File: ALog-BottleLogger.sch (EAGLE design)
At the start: 103 parts, among them IC2 ATMEGA644M, J6 5.5x2.1mm Barrel, Q1 220mA/50V/3.5Ω, Q4 220mA/50V/3.5Ω, Q5 4.3A/20V/54mΩ, Q6 4.3A/20V/54mΩ, Q7 4.3A/20V/54mΩ, Q8 220mA/50V/3.5Ω, Q9 220mA/50V/3.5Ω, U2 FT231X-Q

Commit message: latest design files
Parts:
- removed R20, R22, R44, R45, R5: 10k, rcl:R-EU_R0603
- added ADECOUP: 0.1uF, resistor:C-EUC0603
- added C3, C5, C6: 0.1uF, rcl:C-EUC0603
- added L_LPF: 10uH, SparkFun:INDUCTOR0805
- Q4: value 220mA/50V/3.5Ω -> 4.3A/20V/54mΩ; device SparkFun-DiscreteSemi:MOSFET-NCH-BSS138 -> SparkFun-DiscreteSemi:MOSFET_PCH-IRLML2244
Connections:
- net AIN1 renamed 3
- net CLKO/T1 renamed 1
- net N$41 renamed REF_EN
- net N$56 renamed 30
- net SS renamed SS/4
- net TCK renamed 26
- net TDI renamed 29
- net TDO renamed 28
- net TMS renamed 27
- net XCK0/T0 renamed 0
- removed net +3V2: Q4.G
- removed net 5V: U$7.REF+
- removed net INT2: IC2.(PCINT10/INT2/AIN0)PB2
- removed net N$10: U$2.OUTF
- removed net N$15: U$2.OUTS
- removed net N$16: U$2.VIN
- removed net N$27: RN1A.1, U2.TXD
- removed net N$32: LED2.A, RN1D.1
- removed net N$34: LED1.A, RN1C.1
- removed net USB_STATUS: MICRO_USB.ID
- new net 1.8V_REF: C6.1, IC2.AREF, U$2.OUTF, U$2.OUTS, U$7.CH15
- new net AVCC: ADECOUP.1, IC2.AVCC, L_LPF.2
- new net MISO/6: IC2.(PCINT14/MISO)PB6
- new net MOSI/5: IC2.(PCINT13/MOSI)PB5
- new net N$2: LED2.A, RN1A.1
- new net N$3: LED1.A, RN1D.1
- new net N$4: RN1C.1, U2.TXD
- new net SCK/7: IC2.(PCINT15/SCK)PB7
- net +3V3: now also C5.1, L_LPF.1, U$2.VIN, U$7.CH14; no longer IC2.AREF, IC2.AVCC, R20.1, R22.1, R44.2, R5.2
- net +5V: now also Q4.S, U$7.REF+; no longer U2.VCC
- net 3.3V_EXT_CTRL: no longer R20.2
- net 5V_EXT_CTRL: no longer R5.1
- net ADC14: no longer U$7.CH14
- net ADC15: no longer R44.1, R45.2, U$7.CH15
- net GND: now also ADECOUP.2, C3.2, C5.2, C6.2; no longer R45.1
- net MANUAL_LOG: now also IC2.(PCINT23/TOSC2)PC7
- net MISO: no longer IC2.(PCINT14/MISO)PB6
- net MOSI: no longer IC2.(PCINT13/MOSI)PB5
- net N$40: now also C3.1
- net RTC_INT: now also IC2.(PCINT10/INT2/AIN0)PB2
- net RX_USB: now also RN1C.2; no longer RN1A.2
- net SCK: no longer IC2.(PCINT15/SCK)PB7
- net SD_VCC_CTRL: no longer R22.2
- net VUSB: now also Q4.D, Q4.G, RN1A.2, U2.VCC; no longer RN1C.2
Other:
- note added: "1.8V REFERENCE VOLTAGE"
- note added: "Adjust resistors for 1.8V ADC"
- note added: "Control line for REF_EN"
- note added: "I can control this with the internal pullup"
- note added: "Interrupt on RTC grounds the interrupt pin, otherwise the pin is floating and needs an external pullup."
- note added: "Pin change int or external level int can both wake up logger from power down. But toggle pin must remain in its toggled state until device has woken up to geterate the interrupt."
- note removed: "Adjust resistors for 3.3V ADC"
- moved on the sheet: MICRO_USB, RN1A, RN1C, RN1D

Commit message: progress
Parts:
- removed J5: (no value), SparkFun-Connectors:CONN_10
- removed LED: (no value), SparkFun-LED:LED1206
- removed R_LED: 220, resistor:R-US_R0603
- added LED3: (no value), SparkFun-LED:LED1206
- added R_LED1: 220, resistor:R-US_R0603
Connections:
- net 26 renamed SD-VCC_CTRL
- net 27 renamed D19
- net 29 renamed D21
- net 3 renamed D3
- net SS/4 renamed SS/D4
- removed net 0: IC2.(PCINT8/XCK0/T0)PB0
- removed net 1: IC2.(PCINT9/CLKO/T1)PB1
- removed net 28: IC2.(PCINT20/TDO)PC4
- removed net 30: IC2.(PCINT22/TOSC1)PC6
- removed net EXT_3.3V1: J14.4, J15.4, J16.7, J8.7
- removed net GND3: J14.3, J15.3, J16.6, J8.6
- removed net LED: IC2.(PCINT31/OC2A)PD7, R_LED.1
- removed net LED+: LED.A, R_LED.2
- removed net MISO/6: IC2.(PCINT14/MISO)PB6
- removed net MOSI/5: IC2.(PCINT13/MOSI)PB5
- removed net SCK/7: IC2.(PCINT15/SCK)PB7
- new net D1: IC2.(PCINT9/CLKO/T1)PB1, J2.9
- new net D12: IC2.(PCINT28/OC1B)PD4, J1.3
- new net D13: IC2.(PCINT29/OC1A)PD5, J1.4
- new net D14: IC2.(PCINT30/OC2B/ICP)PD6, J1.8
- new net D15: IC2.(PCINT31/OC2A)PD7, J2.10
- new net D3~: J2.8
- new net LED+1: LED3.A, R_LED1.2
- new net MISO/D6: IC2.(PCINT14/MISO)PB6, ISP2.MISO
- new net MOSI/D5: IC2.(PCINT13/MOSI)PB5, ISP2.MOSI
- new net N$5: IC2.(PCINT8/XCK0/T0)PB0, R_LED1.1
- new net SCK/D7: IC2.(PCINT15/SCK)PB7, ISP2.SCK
- new net SS: J2.4
- net 3.3V_EXT_CTRL: now also IC2.(PCINT22/TOSC1)PC6; no longer IC2.(PCINT30/OC2B/ICP)PD6
- net 5V_EXT_CTRL: now also IC2.(PCINT20/TDO)PC4; no longer IC2.(PCINT29/OC1A)PD5
- net EXT_3.3V: now also J1.6, J14.4, J15.4, J16.7, J2.6, J8.7
- net EXT_5V: now also J1.7, J2.7
- net GND: now also J1.5, J14.3, J15.3, J16.6, J2.5, J8.6, LED3.C; no longer LED.C
- net MISO: now also J2.2; no longer ISP2.MISO
- net MOSI: now also J2.3; no longer ISP2.MOSI
- net RX/INT0: now also J1.1
- net SCK: now also J2.1; no longer ISP2.SCK
- net SCL: now also J1.9
- net SDA: now also J1.10
- net SD_VCC_CTRL: no longer IC2.(PCINT28/OC1B)PD4
- net TX/INT1: now also J1.2
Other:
- note removed: "NOTE: Add 4 GPIO lines"

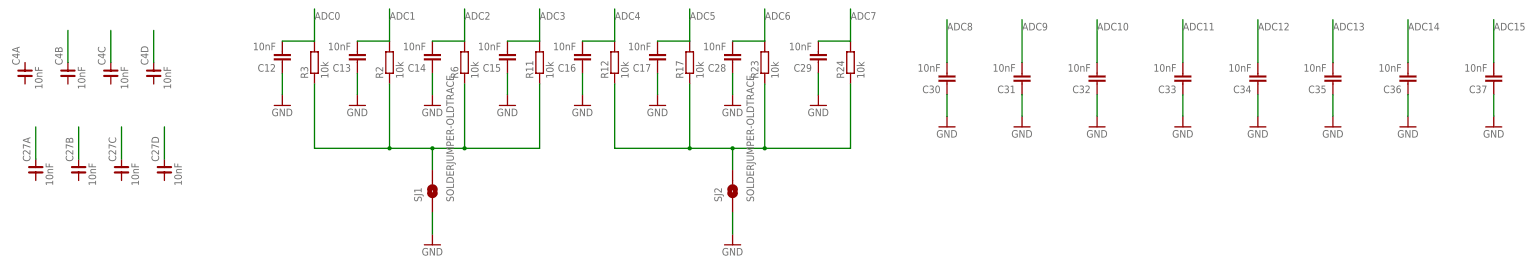
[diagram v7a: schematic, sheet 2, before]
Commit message: 4.75 inches long, reference voltages broken out
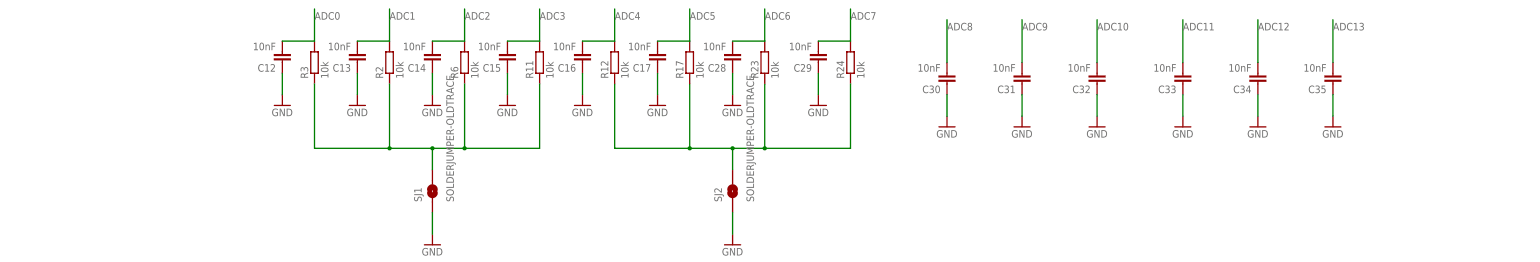
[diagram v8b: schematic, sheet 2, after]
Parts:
- removed C27, C4: 10nF, rc-master-smd:CCA_
- removed C36, C37: 10nF, rcl:C-EUC0603
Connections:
- net D12 renamed D12~
- net D13 renamed D13~
- net D14 renamed D14~
- net D15 renamed D15~
- removed net ADC14: C36.2, J14.2
- removed net ADC15: C37.2, J14.1
- removed net D19: IC2.(PCINT19/TMS)PC3
- removed net D3: IC2.(PCINT11/OC0A/AIN1)PB3
- removed net GND2: C4B.2, C4D.2
- removed net GND4: C27A.2, C27B.2, C27C.2, C27D.2
- removed net N$14: C4C.2
- removed net REF_EN: U$2.EN
- removed net SD-VCC_CTRL: IC2.(PCINT18/TCK)PC2
- removed net SS: J2.4
- new net 1.8V_EN: IC2.(PCINT19/TMS)PC3, U$2.EN
- net +3V3: now also J14.2
- net 1.8V_REF: now also J14.1
- net D1: no longer J2.9
- net D3~: now also IC2.(PCINT11/OC0A/AIN1)PB3
- net GND: no longer C36.1, C37.1
- net MCU_ADC0: now also J2.9
- net MISO: no longer J2.2
- net MISO/D6: now also J2.2
- net MOSI: no longer J2.3
- net MOSI/D5: now also J2.3
- net SCK: no longer J2.1
- net SCK/D7: now also J2.1
- net SD_VCC_CTRL: now also IC2.(PCINT18/TCK)PC2
- net SS/D4: now also J2.4
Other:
- moved on the sheet: C3, C5
